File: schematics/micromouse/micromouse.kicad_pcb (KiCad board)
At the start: 2 copper layers, 70 x 90 mm, 61 parts, among them J1 TOF_LEFT, J10 MotorB_Conn, J11 BMI_ConnB, J12 BMI_ConnA, J13 StepDown_{In+}, J14 StepDown_{In-}, J15 StepDown_{Out+}, J16 StepDown_{Out-}, J2 TOF_FRONTLEFT, J3 TOF_FRONTRIGHT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

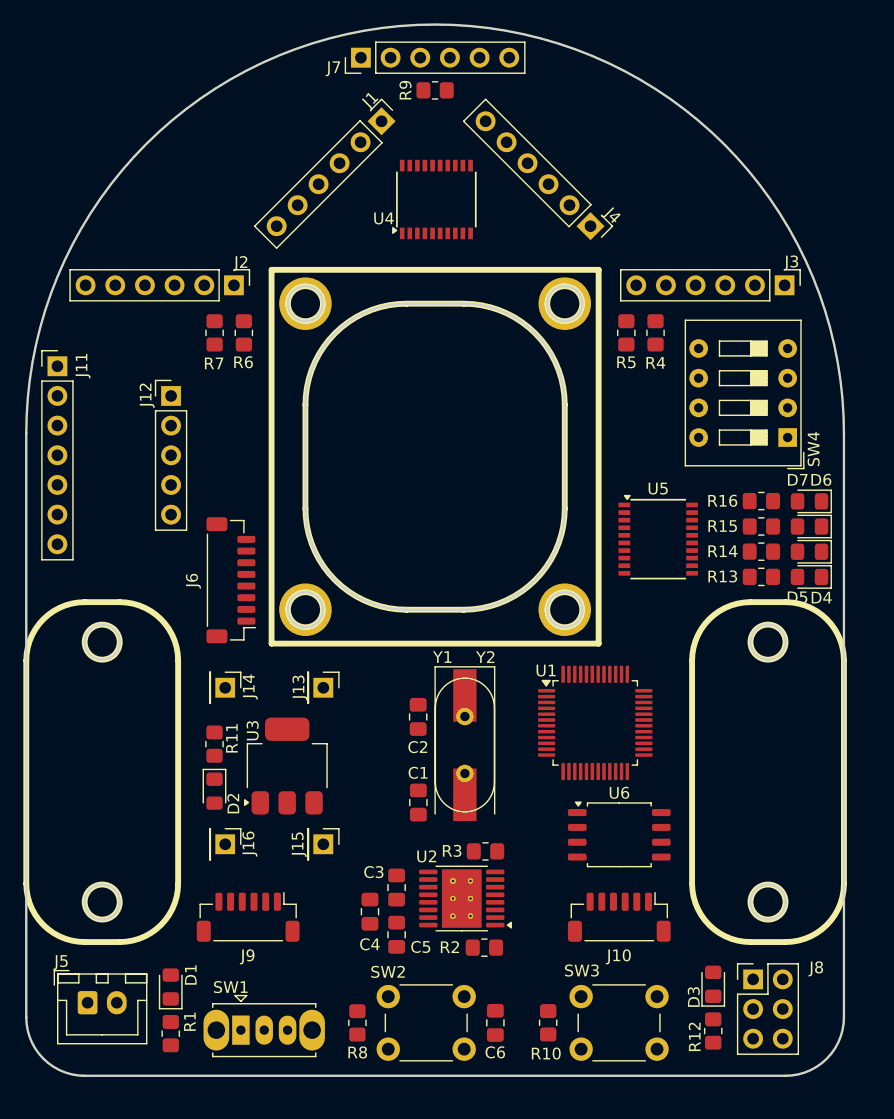
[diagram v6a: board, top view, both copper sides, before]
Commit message: Schematic: * Reorganize STM32 pinout due to Software needs/mititations * Add PCB power protection diodes for Battery port and  Programming port.
PCB:
* Redistribute all lines
* Avoid Crystal zone with SPI/I2C lines
* Add text for element's pinouts

TODO: Add Test Points for signals?
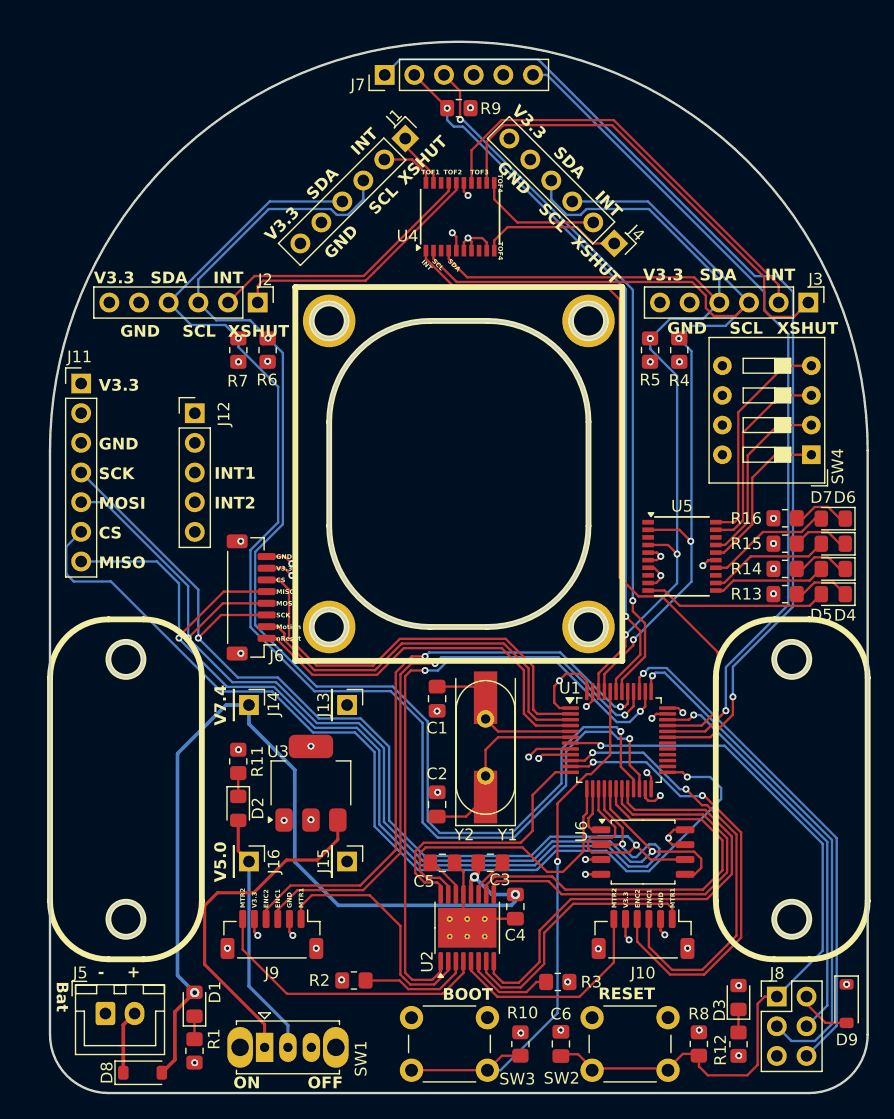
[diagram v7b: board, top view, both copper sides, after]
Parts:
- added D8: D_Schottky, Diode_SMD:D_SOD-123, F.Cu at (113.3, 111.7)
- added D9: D_Schottky, Diode_SMD:D_SOD-123, F.Cu at (173.6, 105.7)
- moved R8 29.3 mm to (161.0, 109.2), turned to 90 degrees
- moved R3 12.8 mm to (148.9, 103.9), turned to 180 degrees
- moved C4 12.5 mm to (145.2, 97.4)
- moved R2 11.5 mm to (131.4, 103.8)
- moved SW2 11.3 mm to (151.8, 106.9), turned to 0 degrees
- moved SW3 10.2 mm to (142.9, 111.4), turned to 180 degrees
- moved C1 9.04 mm to (138.6, 79.6), turned to 90 degrees
- moved C3 8.31 mm to (143.1, 93.7), turned to 180 degrees
- moved C2 7.66 mm to (138.6, 88.7), turned to 90 degrees
- moved C5 7.30 mm to (139.0, 93.7), turned to 0 degrees
- moved C6 5.89 mm to (149.2, 109.2), turned to 90 degrees
- moved Y2 5.39 mm to (142.7, 86.2), turned to 90 degrees
- moved R10 3.00 mm to (145.7, 109.2), turned to -90 degrees
- moved U2 2.55 mm to (141.1, 99.2), turned to 90 degrees
- moved R9 2.54 mm to (140.4, 29.1), turned to 0 degrees
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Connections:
- net /PB3 renamed /SWo
- C3 pad 2: VCC_{7,4} -> VCC_{7.4}
- C4 pad 1: VCC_{7,4} -> VCC_{7.4}
- J5 pad 2: VCC_{7.4} -> Net-(D8-K)
- J8 pad 2: VCC_{3.3} -> Net-(D9-A)
- R9 pad 1: VCC_{3.3} -> /USART1_{RX}
- R9 pad 2: /USART1_{RX} -> VCC_{3.3}
- U1 pad 10: unconnected-(U1-PA0-Pad10) -> /ENCODERA_{C1}
- U1 pad 11: unconnected-(U1-PA1-Pad11) -> /ENCODERA_{C2}
- U1 pad 12: unconnected-(U1-PA2-Pad12) -> /MOTOR_{a1}
- U1 pad 13: unconnected-(U1-PA3-Pad13) -> /MOTOR_{a2}
- U1 pad 14: unconnected-(U1-PA4-Pad14) -> /FLASH_{cs}
- U1 pad 18: unconnected-(U1-PB0-Pad18) -> /MOTOR_{b2}
- U1 pad 19: unconnected-(U1-PB1-Pad19) -> /MOTOR_{b1}
- U1 pad 2: unconnected-(U1-PC13-Pad2) -> /PMW_{cs}
- U1 pad 20: unconnected-(U1-PB2-Pad20) -> /MOTOR_{fault}
- U1 pad 25: unconnected-(U1-PB12-Pad25) -> /BMI_{cs}
- U1 pad 29: /PMW_{cs} -> unconnected-(U1-PA8-Pad29)
- U1 pad 3: unconnected-(U1-PC14-Pad3) -> /PMW_{motion}
- U1 pad 30: /USART1_{TX} -> unconnected-(U1-PA9-Pad30)
- U1 pad 31: /USART1_{RX} -> /BT_{state}
- U1 pad 32: unconnected-(U1-PA11-Pad32) -> /BT_{enable}
- U1 pad 33: unconnected-(U1-PA12-Pad33) -> /TOF_{int}
- U1 pad 38: unconnected-(U1-PA15-Pad38) -> /MOTOR_{sleep}
- U1 pad 4: unconnected-(U1-PC15-Pad4) -> /PMW_{nreset}
- U1 pad 40: unconnected-(U1-PB4-Pad40) -> /ENCODERB_{C1}
- U1 pad 41: unconnected-(U1-PB5-Pad41) -> /ENCODERB_{C2}
- U1 pad 42: /I2C1_{scl} -> /USART1_{TX}
- U1 pad 43: /I2C1_{sda} -> /USART1_{RX}
- U1 pad 45: unconnected-(U1-PB8-Pad45) -> /I2C1_{scl}
- U1 pad 46: unconnected-(U1-PB9-Pad46) -> /I2C1_{sda}
- U2 pad 12: VCC_{7,4} -> VCC_{7.4}
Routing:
- net /I2C2_{scl}: track 0.00 -> 108.9 mm, vias 0 -> 2
- net /I2C2_{sda}: track 0.00 -> 108.1 mm, vias 0 -> 2
- net /I2C1_{scl}: track 0.00 -> 94.7 mm, vias 0 -> 3
- net /SPI1_{clk}: track 0.00 -> 94.7 mm, vias 0 -> 2
- net /SPI1_{mosi}: track 0.00 -> 91.6 mm, vias 0 -> 2
- net /I2C1_{sda}: track 0.00 -> 90.6 mm, vias 0 -> 3
- net /SPI1_{miso}: track 0.00 -> 90.4 mm, vias 0 -> 2
- net /BT_{state}: track 0.00 -> 88.9 mm, vias 0 -> 1
- net /BMI_{cs}: track 0.00 -> 84.5 mm, vias 0 -> 1
- net VCC_{7.4}: track 0.00 -> 80.3 mm, vias 0 -> 3
- net /BT_{enable}: track 0.00 -> 72.9 mm, vias 0 -> 1
- net /RESET: track 0.00 -> 66.5 mm, vias 0 -> 1
- net /TOF_{int}: track 0.00 -> 63.3 mm
- net /USART1_{RX}: track 0.00 -> 62.3 mm, vias 0 -> 2
- net /USART1_{TX}: track 0.00 -> 60.9 mm, vias 0 -> 2
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- added copper zone on In1.Cu, net GND
- added copper zone on In2.Cu, net VCC_{3.3}
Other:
- outline, holes or cut-outs redrawn
- copper layers 2 -> 4
- board text added: "+"
- board text added: "-"
- board text added: "BOOT"
- board text added: "Bat"
- board text added: "CS"
- board text added: "ENC1"
- board text added: "ENC2"
- board text added: "GND"
- board text added: "INT"
- board text added: "INT1"
- board text added: "INT2"
- board text added: "MISO"
- board text added: "MOSI"
- board text added: "MTR1"
- board text added: "MTR2"
- board text added: "Motion"
- board text added: "OFF"
- board text added: "ON"
- board text added: "RESET"
- board text added: "SCK"
- board text added: "SCL"
- board text added: "SDA"
- board text added: "TOF1"
- board text added: "TOF2"
- board text added: "TOF3"
- board text added: "TOF4"
- board text added: "V3.3"
- board text added: "V5.0"
- board text added: "V7.4"
- board text added: "XSHUT"
- board text added: "nReset"

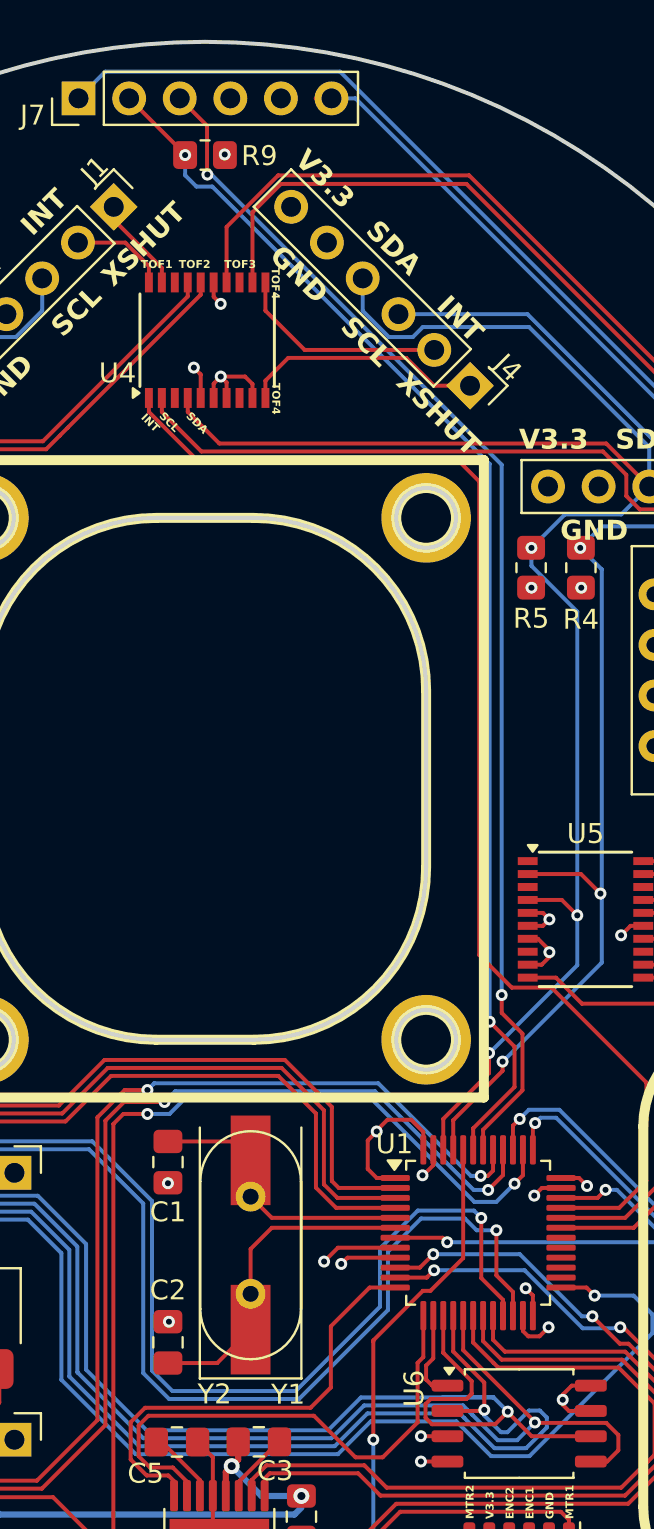
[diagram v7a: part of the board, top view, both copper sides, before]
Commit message: Schematic/PCB: Add missing resistor for Crystal, based on STM's AN2586 (Getting started with STM32F10xxx hardware development).
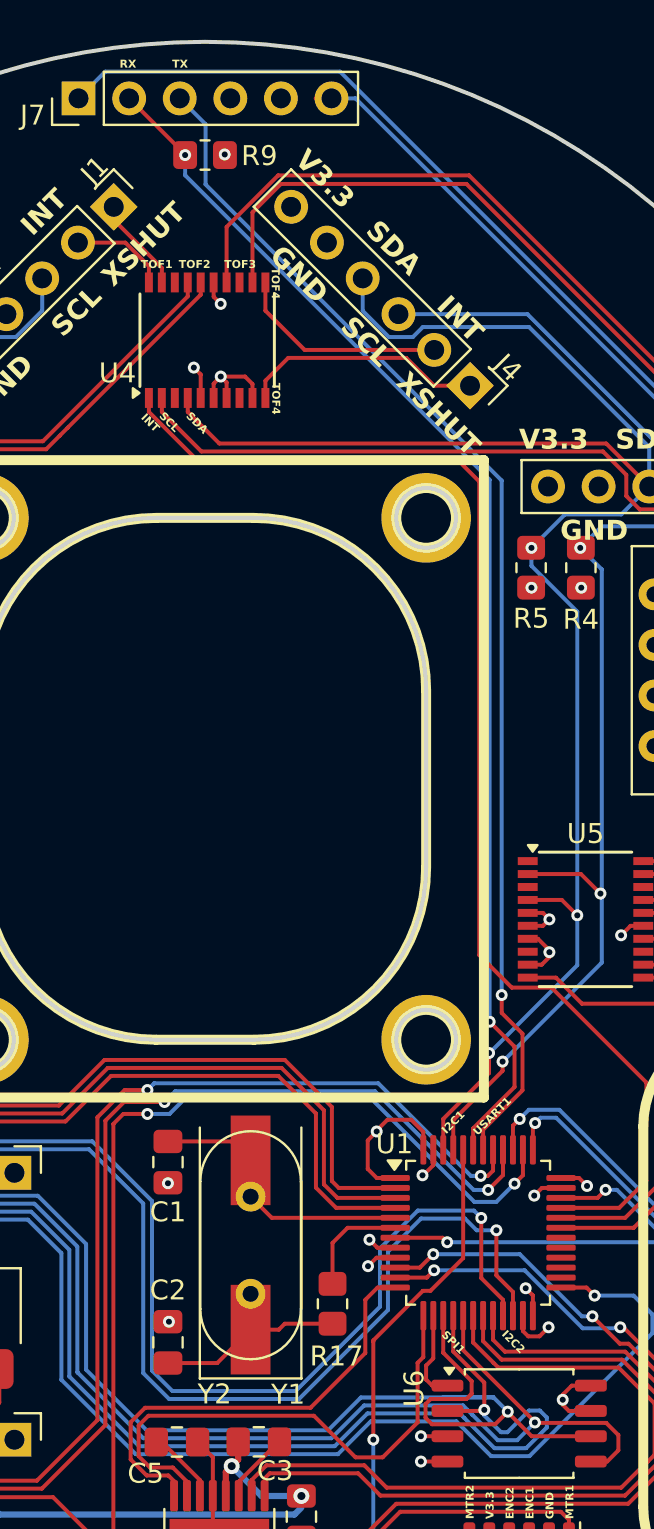
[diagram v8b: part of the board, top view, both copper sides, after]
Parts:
- added R17: 200m, Resistor_SMD:R_0805_2012Metric_Pad1.20x1.40mm_HandSolder, F.Cu at (146.8, 86.8)
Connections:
- C2 pad 1: Net-(U1-PD1) -> Net-(C2-Pad1)
- Y1 pad 1: Net-(U1-PD1) -> Net-(C2-Pad1)
- Y2 pad 1: Net-(U1-PD1) -> Net-(C2-Pad1)
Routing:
- net Net-(U1-PD1): track 14.8 -> 5.52 mm
- net Net-(C2-Pad1): track 0.00 -> 9.08 mm
- net GND: track 34.6 -> 32.2 mm
- net VCC_{3.3}: track 27.9 -> 26.6 mm
- net /USART1_{TX}: track 60.9 -> 60.7 mm, vias 2 -> 1
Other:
- board text added: "I2C1"
- board text added: "I2C2"
- board text added: "RX"
- board text added: "SPI1"
- board text added: "TX"
- board text added: "USART1"
